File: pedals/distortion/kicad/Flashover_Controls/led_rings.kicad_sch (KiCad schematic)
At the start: 43 parts, among them U10 IS31FL3236A

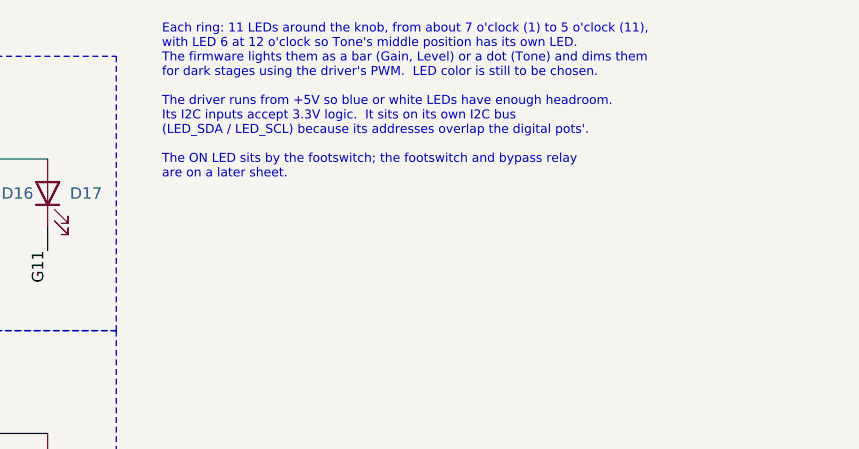
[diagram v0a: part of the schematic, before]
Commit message: Split Flashover into main and control boards; place parts
Main board (Flashover): audio, controller, pots, MIDI, bypass and the five
top-mounted jacks.  Control board (Flashover_Controls): encoders, LED rings,
LED driver, Soft/Hard button and panel LEDs.  J7/J8 2x10 board connector,
M3 mounting holes, regulator laid flat.  Placement only, not yet routed.

Co-Authored-By: Claude Opus 5.5 <noreply@anthropic.com>
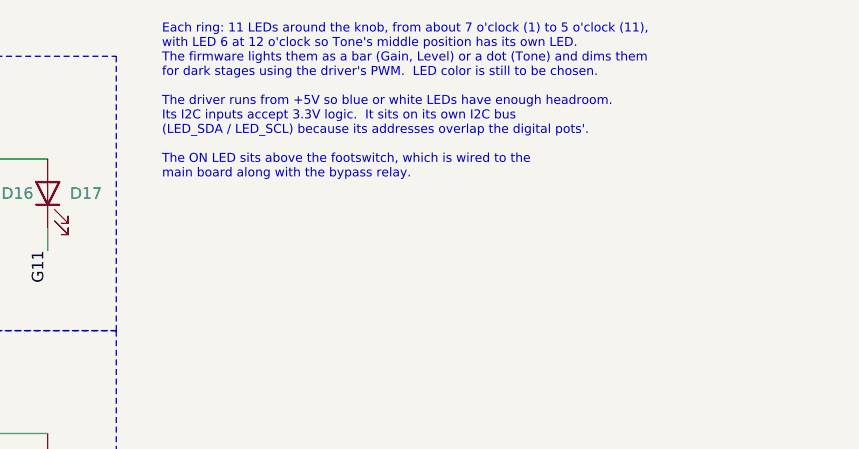
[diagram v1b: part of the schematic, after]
